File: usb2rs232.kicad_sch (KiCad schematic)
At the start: 19 parts, among them J3 USB_C_Receptacle_USB2.0_14P, Q4 L8050QLT1G, Q5 L8050QLT1G, U5 CP2102N-Axx-xQFN28

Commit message: Add input protection, fix USB-C/CP2102 supply, harden optocoupler input
Power supply:
- Add 12V input protection: PTC fuse F1 (1.1A/33V, C70119), TVS D6
  (SMAJ15CA, C151939), reverse polarity Schottky D7 (SS34, C8678) and
  bulk cap C13 (100uF/25V, C179802)

USB2RS232:
- Power CP2102N (VDD/REGIN) from +3.3V via R25 (0R)
- Add 5k1 pull-downs R23/R24 on USB-C CC1/CC2 so C-to-C hosts supply VBUS

ESP32 / Interfaces:
- Add 100k gate pull-downs R26/R27/R28 on Q2/Q1/Q3 (relay, LED, buzzer
  stay off during reset/boot)
- Buzzer flyback D1: 1N4148W SOD-123 (C81598) instead of undefined SOT-23
- WAKE_UP input (J8/U3): series zener D8 (BZT52C6V8, C173404), reverse
  polarity diode D9 (1N4148W), R11 = 1k5 0805 (C4310); switches at ~9V,
  safe up to 14.4V
- IC1 value set to ESP32-S3-WROOM-1U to match footprint
- Add no-connect flags on unused ESP32, J99 and K1 pins
- Remove duplicate local labels IO_PUMP_LED/IO_PUMP_RELAIS
- Move off-grid symbols, labels and wires onto grid

PCB: update from schematic
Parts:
- added R23, R24: 5k1, Resistor_SMD:R_0603_1608Metric_Pad0.98x0.95mm_HandSolder, symbol Device:R
- added R25: 0R, Resistor_SMD:R_0402_1005Metric_Pad0.72x0.64mm_HandSolder, symbol Device:R
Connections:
- net CP2102_3V3: now also R25.1
- net GND: now also R23.2, R24.2
- net at J3.A5 (CC1): now also R23.1
- net at J3.B5 (CC2): now also R24.1
- new net +3.3V: R25.2

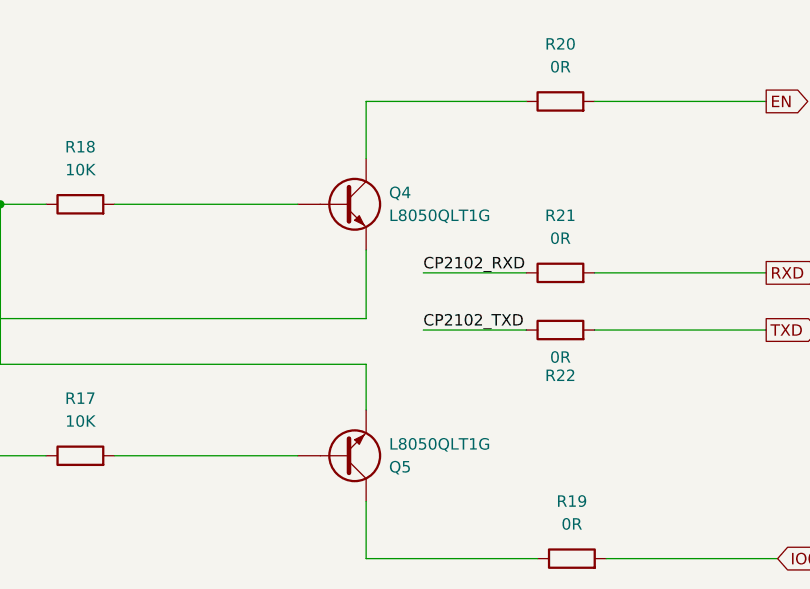
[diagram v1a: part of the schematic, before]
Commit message: - Q4/Q5: use MMBT3904 symbol (numbered pins) so SOT-23 pads map correctly
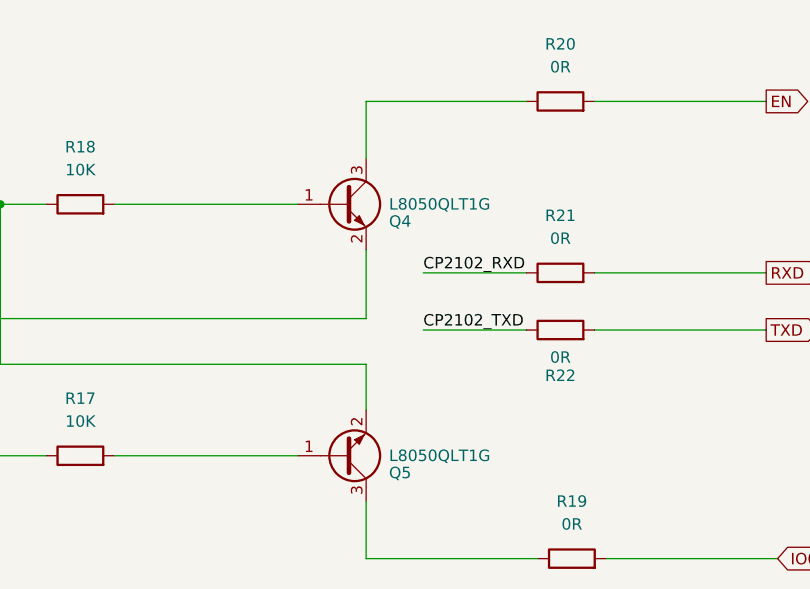
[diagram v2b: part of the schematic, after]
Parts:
- removed Q4, Q5: L8050QLT1G, Package_TO_SOT_SMD:SOT-23, symbol Device:Q_NPN
- added Q4, Q5: L8050QLT1G, Package_TO_SOT_SMD:SOT-23, symbol Transistor_BJT:MMBT3904
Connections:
- net CP2102_DTR: now also Q5.2 (E)
- net CP2102_RTS: now also Q4.2 (E)
- net at R19.1: now also Q5.3 (C)
- net at R20.1: now also Q4.3 (C)
- net at R18.2: now also Q4.1 (B)
- net at R17.2: now also Q5.1 (B)
